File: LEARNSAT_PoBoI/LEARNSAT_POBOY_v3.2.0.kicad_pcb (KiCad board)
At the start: 4 copper layers, 90.2 x 95.8 mm, 489 parts, among them J1 FTSH-105-01-L-DV-K-P-TR, J5 FTSH-105-01-L-DV-K-P-TR, P1 22-28-4036, Q1 SI7164DP-T1-GE3, Q10 SI5418DU-T1-GE3, Q11 SI7164DP-T1-GE3, Q12 SI5418DU-T1-GE3, Q13 SI5418DU-T1-GE3, Q13 SI7164DP-T1-GE3, Q14 SI5418DU-T1-GE3, Q14 SI7164DP-T1-GE3, Q15 SI7164DP-T1-GE3, Q16 SI5418DU-T1-GE3, Q17 SI7164DP-T1-GE3, Q18 SI5418DU-T1-GE3, Q19 SI7164DP-T1-GE3, Q2 SI7164DP-T1-GE3, Q20 SI5418DU-T1-GE3, Q20 SI7164DP-T1-GE3, Q21 SI7164DP-T1-GE3, Q22 SI5418DU-T1-GE3, Q23 SI7164DP-T1-GE3, Q24 SI5418DU-T1-GE3, Q3 SI7164DP-T1-GE3, Q4 SI5418DU-T1-GE3, Q5 SI5418DU-T1-GE3, Q6 SI7164DP-T1-GE3, Q7 SI7164DP-T1-GE3, Q8 SI5418DU-T1-GE3, Q9 SI5418DU-T1-GE3, SW1 B3U-1000P, SW2 B3U-1000P, SW3 TS04-66-43-BK-100-SMT, U1 MAX6746KA29+T, U1 STM32F103RET6, U10 LM2622MMX-ADJ/NOPB, U11 LM2622MMX-ADJ/NOPB, U12 INA219AIDCNR, U13 INA219AIDCNR, U14 INA219AIDCNR, U15 LTC4231IUD-2#TRPBF, U16 LTC4231IUD-2#TRPBF, U17 LP5907SNX-3.3, U18 LP5907SNX-3.3, U18 LTC4231IUD-2#TRPBF, U19 INA219AIDCNR, U2 SN74AUP1G08QDCKRQ1, U20 INA219AIDCNR, U21 74AC14MTCX, U22 LTC4231IUD-2#TRPBF, U22 LTC4304CMS#PBF, U23 INA219AIDCNR, U23 SN74LVC1G373DCKR, U24 LTC4231IUD-2#TRPBF, U25 INA219AIDCNR, U25 LTC4231IUD-2#TRPBF, U26 ISL3259EIRZ, U26 LTC4231IUD-2#TRPBF, U27 INA219AIDCNR, U28 LTC4231IUD-2#TRPBF, U29 INA219AIDCNR, U29 LTC4231IUD-2#TRPBF, U3 MAX6746KA29+T, U30 INA219AIDCNR, U30 LTC4231IUD-2#TRPBF, U31 INA219AIDCNR, U32 LTC4231IUD-2#TRPBF, U33 INA219AIDCNR, U34 MAX6746KA29+T, U35 MAX6746KA29+T, U36 SN74AUP1G08QDCKRQ1, U37 SN74AUP1G08QDCKRQ1, U38 LTC4304CMS#PBF, U39 74AC14MTCX, U4 SN74AUP1G08QDCKRQ1, U40 SN74LVC1G373DCKR, U41 ISL3259EIRZ, U5 LT1616ES6#TRMPBF, U50 LM2622MMX-ADJ/NOPB, U51 LM2622MMX-ADJ/NOPB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

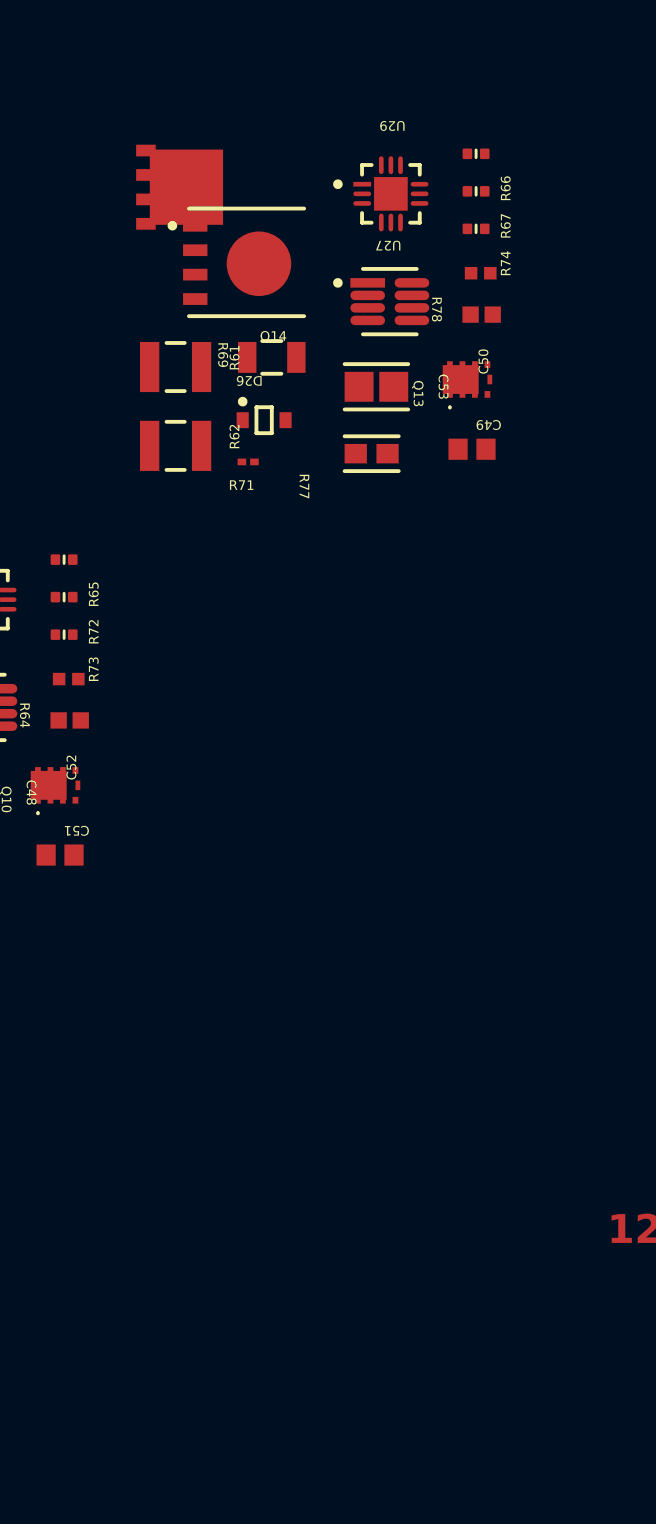
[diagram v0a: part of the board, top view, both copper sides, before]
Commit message: routed VBATTPrimary
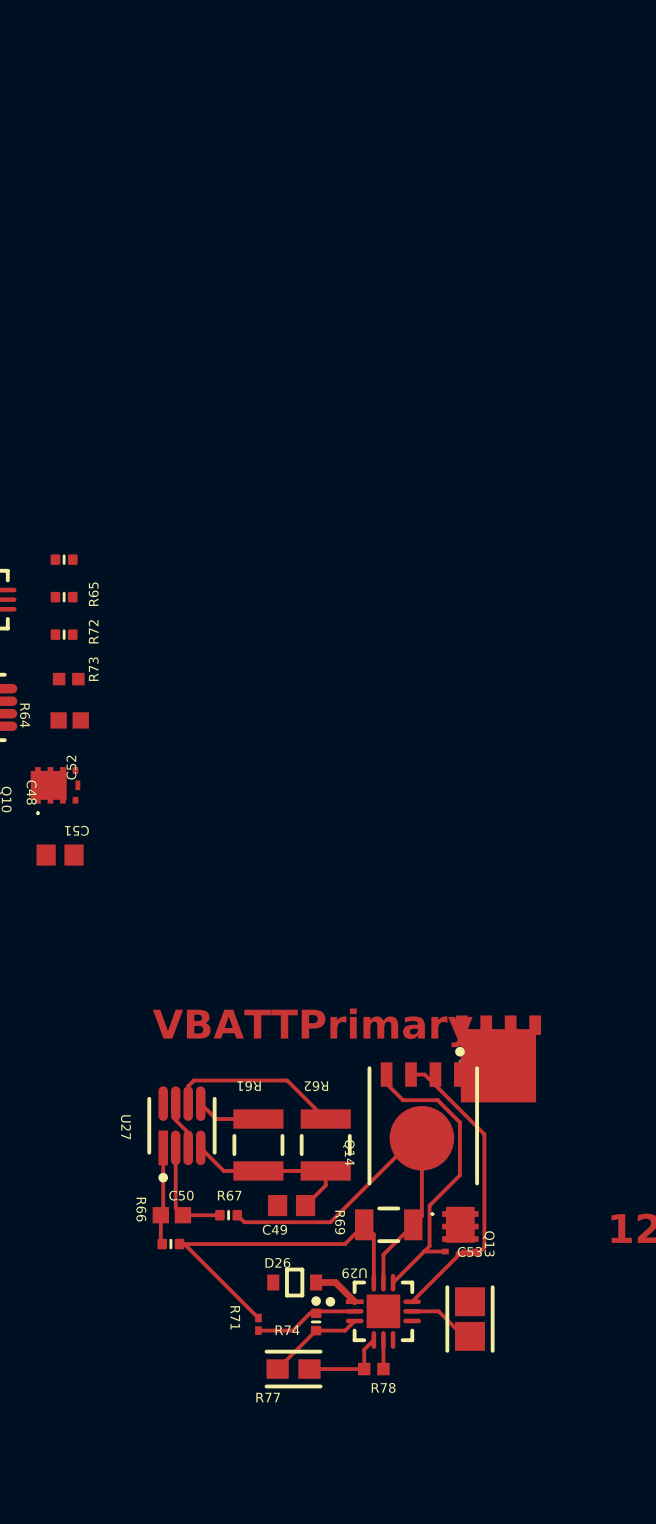
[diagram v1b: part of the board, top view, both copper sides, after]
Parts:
- moved R66 58.9 mm to (189.7, 162.1), turned to 180 degrees
- moved U29 58.1 mm to (200.8, 165.6)
- moved R74 57.4 mm to (197.3, 166.1), turned to -90 degrees
- moved R78 57.2 mm to (200.3, 168.6)
- moved R67 54.8 mm to (192.7, 160.6), turned to 180 degrees
- moved C50 49.5 mm to (189.8, 160.6), turned to 180 degrees
- moved C53 48.7 mm to (205.3, 166.0), turned to 90 degrees
- moved R77 47.8 mm to (196.1, 168.6)
- moved Q14 45.8 mm to (202.9, 155.9), turned to -90 degrees
- moved R69 45.5 mm to (201.1, 161.1)
- moved D26 44.9 mm to (196.2, 164.1), turned to 180 degrees
- moved R71 44.8 mm to (194.3, 166.3), turned to -90 degrees
- moved U27 44.2 mm to (190.3, 155.9), turned to 90 degrees
- moved Q13 44.0 mm to (204.7, 161.2), turned to -90 degrees
- moved R61 40.7 mm to (194.3, 156.9), turned to 90 degrees
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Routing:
- net Net-(Q14-D): track 0.00 -> 19.9 mm
- net /VBATT PRIMARY/VBATT: track 0.00 -> 18.9 mm
- net Net-(Q13-S_1): track 0.00 -> 17.3 mm
- net Net-(Q13-G): track 0.00 -> 16.0 mm
- net 3V3: track 58.6 -> 67.9 mm
- net SDA: track 28.9 -> 37.9 mm
- net Net-(U27-IN-): track 0.00 -> 5.58 mm
- net Net-(U29-UVL): track 0.00 -> 5.42 mm
- net Net-(U27-IN+): track 0.00 -> 5.08 mm
- net Net-(U29-UVH): track 0.00 -> 5.05 mm
- net Net-(U29-OV): track 0.00 -> 4.56 mm
- net Net-(U29-TIMER): track 0.00 -> 3.55 mm
- net SCL: track 25.5 -> 28.8 mm
- net GND: track 272.3 -> 274.8 mm
- net /VBATT PRIMARY/VBatt_EnableP: track 0.00 -> 2.42 mm
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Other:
- board text added: "VBATTPrimary"
